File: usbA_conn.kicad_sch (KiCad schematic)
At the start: 3 parts, among them J1 USB2

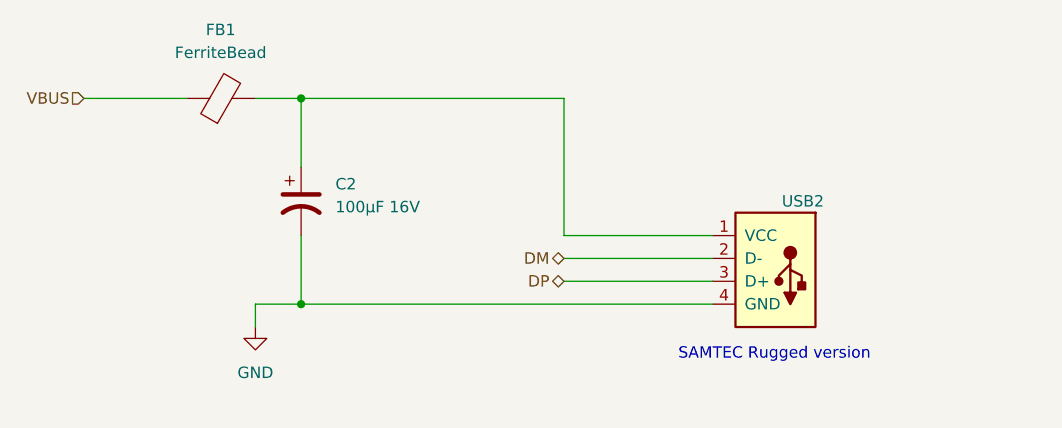
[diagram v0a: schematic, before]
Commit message: Finished schematic
The USB-A connector foortprint, 3D model, and symbol comes from Snap
EDA.
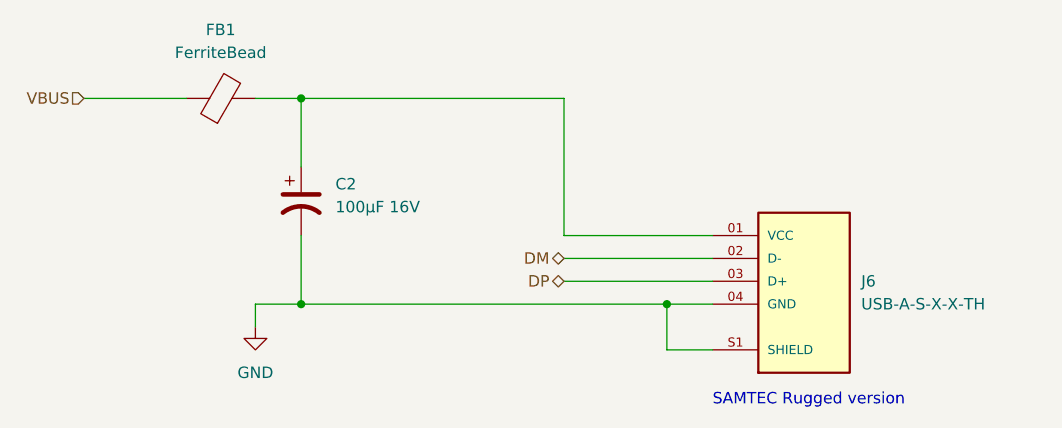
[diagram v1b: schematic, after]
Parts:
- removed J1: USB2, symbol Connector:USB_A
- added J6: USB-A-S-X-X-TH, USB-A-S-X-X-TH:SAMTEC_USB-A-S-X-X-TH, symbol USB-A-S-X-X-TH:USB-A-S-X-X-TH
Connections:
- net DM: now also J6.02 (D-)
- net DP: now also J6.03 (D+)
- net GND: now also J6.04 (GND), J6.S1 (SHIELD), J6.S2 (SHIELD)
- net at C2.1, FB1.2: now also J6.01 (VCC)
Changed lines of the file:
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@@
   (junction (at 106.68 72.39) (diameter 0) (color 0 0 0 0)
   )
+  (junction (at 147.32 95.25) (diameter 0) (color 0 0 0 0)
+  )
   (wire (pts (xy 101.6 72.39) (xy 106.68 72.39))
     (stroke (width 0) (type default))
@@
     (stroke (width 0) (type default))
   )
+  (wire (pts (xy 147.32 100.33) (xy 147.32 95.25))
+    (stroke (width 0) (type default))
+  )
   (wire (pts (xy 82.55 72.39) (xy 93.98 72.39))
     (stroke (width 0) (type default))
@@
     (stroke (width 0) (type default))
   )
+  (wire (pts (xy 147.32 95.25) (xy 152.4 95.25))
+    (stroke (width 0) (type default))
+  )
   (wire (pts (xy 135.89 87.63) (xy 135.89 72.39))
     (stroke (width 0) (type default))
@@
     (stroke (width 0) (type default))
   )
-  (wire (pts (xy 106.68 95.25) (xy 152.4 95.25))
+  (wire (pts (xy 106.68 95.25) (xy 147.32 95.25))
     (stroke (width 0) (type default))
   )
@@
     (stroke (width 0) (type default))
   )
+  (wire (pts (xy 152.4 100.33) (xy 147.32 100.33))
+    (stroke (width 0) (type default))
+  )
   (wire (pts (xy 106.68 72.39) (xy 135.89 72.39))
     (stroke (width 0) (type default))
@@
     (stroke (width 0) (type default))
   )
-  (text "SAMTEC Rugged version" (at 148.59 101.6 0)
+  (text "SAMTEC Rugged version" (at 152.4 106.68 0)
     (effects (font (size 1.27 1.27)) (justify left bottom))
   )
@@
     )
   )
-  (symbol (lib_id "Connector:USB_A") (at 160.02 90.17 0) (mirror y) (unit 1)
-    (in_bom yes) (on_board yes) (dnp no)
-    (property "Reference" "J1" (at 160.02 76.835 0)
-      (effects (font (size 1.27 1.27)) hide)
-    )
-    (property "Value" "USB2" (at 162.433 83.82 0)
-      (effects (font (size 1.27 1.27)))
-    )
-    (property "Footprint" "" (at 156.21 91.44 0)
-      (effects (font (size 1.27 1.27)) hide)
-    )
-    (property "Datasheet" " ~" (at 167.64 93.98 0)
-      (effects (font (size 1.27 1.27)) hide)
-    )
-    (property "FarnellRef" "3664925" (at 160.02 90.17 0)
-      (effects (font (size 1.27 1.27)) hide)
-    )
-    (pin "1")
-    (pin "2")
-    (pin "3")
-    (pin "4")
-    (instances
-      (project "USBHUB_FE1.1S"
-        (path "/fe375ede-0629-4c66-9d75-419b70ed1e04/4f3f80b4-a978-4ca2-a470-b3140a5c4505"
-          (reference "J1") (unit 1)
-        )
-        (path "/fe375ede-0629-4c66-9d75-419b70ed1e04/447b2eb4-c2d3-421d-9cc5-23c41b99c85e"
-          (reference "J2") (unit 1)
-        )
-        (path "/fe375ede-0629-4c66-9d75-419b70ed1e04/b562ac31-279b-46a3-85af-abe0dcd1c571"
-          (reference "J3") (unit 1)
-        )
-        (path "/fe375ede-0629-4c66-9d75-419b70ed1e04/01137795-a0a0-4966-8ecc-f5421f8336d6"
-          (reference "J4") (unit 1)
-        )
-      )
+  (symbol (lib_id "USB-A-S-X-X-TH:USB-A-S-X-X-TH") (at 162.56 92.71 0) (unit 1)
+    (in_bom yes) (on_board yes) (dnp no) (fields_autoplaced)
+    (property "Reference" "J6" (at 168.91 92.71 0)
+      (effects (font (size 1.27 1.27)) (justify left))
+    )
+    (property "Value" "USB-A-S-X-X-TH" (at 168.91 95.25 0)
+      (effects (font (size 1.27 1.27)) (justify left))
+    )
+    (property "Footprint" "USB-A-S-X-X-TH:SAMTEC_USB-A-S-X-X-TH" (at 162.56 92.71 0)
+      (effects (font (size 1.27 1.27)) (justify bottom) hide)
+    )
+    (property "Datasheet" "" (at 162.56 92.71 0)
+      (effects (font (size 1.27 1.27)) hide)
+    )
+    (property "MF" "Samtec Inc." (at 162.56 92.71 0)
+      (effects (font (size 1.27 1.27)) (justify bottom) hide)
+    )
+    (property "MAXIMUM_PACKAGE_HEIGHT" "7.08 mm" (at 162.56 92.71 0)
+      (effects (font (size 1.27 1.27)) (justify bottom) hide)
+    )
+    (property "Package" "None" (at 162.56 92.71 0)
+      (effects (font (size 1.27 1.27)) (justify bottom) hide)
+    )
+    (property "Price" "None" (at 162.56 92.71 0)
+      (effects (font (size 1.27 1.27)) (justify bottom) hide)
+    )
+    (property "Check_prices" "https://www.snapeda.com/parts/USB-A-S-F-B-TH/Samtec+Inc./view-part/?ref=eda" (at 162.56 92.71 0)
+      (effects (font (size 1.27 1.27)) (justify bottom) hide)
+    )
+    (property "STANDARD" "Manufacturer Recommendations" (at 162.56 92.71 0)
+      (effects (font (size 1.27 1.27)) (justify bottom) hide)
+    )
+    (property "PARTREV" "R" (at 162.56 92.71 0)
+      (effects (font (size 1.27 1.27)) (justify bottom) hide)
+    )
+    (property "SnapEDA_Link" "https://www.snapeda.com/parts/USB-A-S-F-B-TH/Samtec+Inc./view-part/?ref=snap" (at 162.56 92.71 0)
+      (effects (font (size 1.27 1.27)) (justify bottom) hide)
+    )
+    (property "MP" "USB-A-S-F-B-TH" (at 162.56 92.71 0)
+      (effects (font (size 1.27 1.27)) (justify bottom) hide)
+    )
+    (property "Description" "\n                        \n                            USB-A (USB TYPE-A) USB 2.0 Receptacle Connector 4 Position Through Hole, Right Angle\n                        \n" (at 162.56 92.71 0)
+      (effects (font (size 1.27 1.27)) (justify bottom) hide)
+    )
+    (property "Availability" "In Stock" (at 162.56 92.71 0)
+      (effects (font (size 1.27 1.27)) (justify bottom) hide)
+    )
+    (property "MANUFACTURER" "Samtec" (at 162.56 92.71 0)
+      (effects (font (size 1.27 1.27)) (justify bottom) hide)
+    )
+    (pin "S2")
+    (pin "S1")
+    (pin "04")
+    (pin "03")
+    (pin "02")
+    (pin "01")
+    (instances
+      (project "USBHUB_FE1.1S"
+        (path "/fe375ede-0629-4c66-9d75-419b70ed1e04/4f3f80b4-a978-4ca2-a470-b3140a5c4505"
+          (reference "J6") (unit 1)
+        )
+        (path "/fe375ede-0629-4c66-9d75-419b70ed1e04/447b2eb4-c2d3-421d-9cc5-23c41b99c85e"
+          (reference "J7") (unit 1)
+        )
+        (path "/fe375ede-0629-4c66-9d75-419b70ed1e04/b562ac31-279b-46a3-85af-abe0dcd1c571"
+          (reference "J8") (unit 1)
+        )
+        (path "/fe375ede-0629-4c66-9d75-419b70ed1e04/01137795-a0a0-4966-8ecc-f5421f8336d6"
+          (reference "J9") (unit 1)
+        )
+      )

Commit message: ERC pass but one ground pin on th eUSB-A connector.
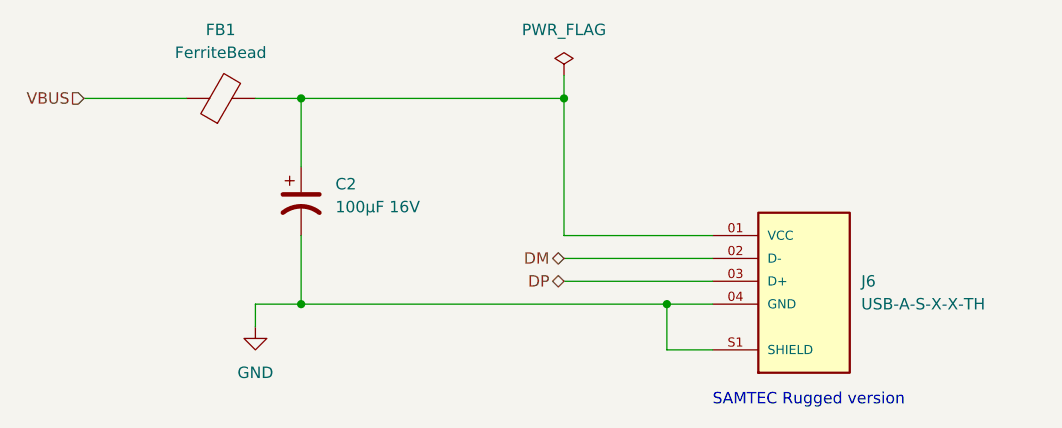
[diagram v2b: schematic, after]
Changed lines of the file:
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@@
 (kicad_sch (version 20230121) (generator eeschema)
   (paper "A4")
+  (junction (at 135.89 72.39) (diameter 0) (color 0 0 0 0)
+  )
   (junction (at 106.68 95.25) (diameter 0) (color 0 0 0 0)
   )
@@
   )
   (wire (pts (xy 135.89 92.71) (xy 152.4 92.71))
+    (stroke (width 0) (type default))
+  )
+  (wire (pts (xy 135.89 69.85) (xy 135.89 72.39))
     (stroke (width 0) (type default))
   )
@@
         )
       )
+    )
+  )
+  (symbol (lib_id "power:PWR_FLAG") (at 135.89 69.85 0) (unit 1)
+    (in_bom yes) (on_board yes) (dnp no) (fields_autoplaced)
+    (property "Reference" "#FLG03" (at 135.89 67.945 0)
+      (effects (font (size 1.27 1.27)) hide)
+    )
+    (property "Value" "PWR_FLAG" (at 135.89 64.77 0)
+      (effects (font (size 1.27 1.27)))
+    )
+    (property "Footprint" "" (at 135.89 69.85 0)
+      (effects (font (size 1.27 1.27)) hide)
+    )
+    (property "Datasheet" "~" (at 135.89 69.85 0)
+      (effects (font (size 1.27 1.27)) hide)
+    )
+    (pin "1")
+    (instances
+      (project "USBHUB_FE1.1S"
+        (path "/fe375ede-0629-4c66-9d75-419b70ed1e04/4f3f80b4-a978-4ca2-a470-b3140a5c4505"
+          (reference "#FLG03") (unit 1)
+        )
+        (path "/fe375ede-0629-4c66-9d75-419b70ed1e04/447b2eb4-c2d3-421d-9cc5-23c41b99c85e"
+          (reference "#FLG04") (unit 1)
+        )
+        (path "/fe375ede-0629-4c66-9d75-419b70ed1e04/b562ac31-279b-46a3-85af-abe0dcd1c571"
+          (reference "#FLG05") (unit 1)
+        )
+        (path "/fe375ede-0629-4c66-9d75-419b70ed1e04/01137795-a0a0-4966-8ecc-f5421f8336d6"
+          (reference "#FLG06") (unit 1)
+        )
+      )

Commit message: Routed, Rev1
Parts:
- J6: footprint USB-A-S-X-X-TH:SAMTEC_USB-A-S-X-X-TH -> lib:SAMTEC_USB-A-S-X-X-TH
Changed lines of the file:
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@@
       (effects (font (size 1.27 1.27)) (justify left))
     )
-    (property "Footprint" "USB-A-S-X-X-TH:SAMTEC_USB-A-S-X-X-TH" (at 162.56 92.71 0)
+    (property "Footprint" "lib:SAMTEC_USB-A-S-X-X-TH" (at 162.56 92.71 0)
       (effects (font (size 1.27 1.27)) (justify bottom) hide)
     )
